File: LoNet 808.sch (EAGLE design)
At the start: 25 parts, among them CN2 JST-2.0, J4 MICRO-SMD, U1 TXB0104PWR

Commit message: add components
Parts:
- added C5: 470uf, Seeed-OPL-Capacitor:TANTALUM-SMD-470UF-6.3V(AVX-D)
- added C6: 220uf, Seeed-OPL-Capacitor:TANTALUM-SMD-220UF-16V(AVX-E)
- added D6: 28V-5A, Seeed-OPL-Diode:SMD-DIODE-SCHOTTKY-28V-5A(DO-214AA)
- added IC1: LM2596S, national-semiconductor:LM2596S
- added J5: DC-005, Seeed-OPL-Connector:CONN-POWER-JACK-2.1MM(DC-005)
- added L2: 22UH, Seeed-OPL-Inductor:SMD-INDUCTOR-22UH-20%(2P-2.0X1.2MM)
- added U2: (no value), LBRmicrobuilder:MCP73831/2
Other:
- note removed: "MICRO USB INTERFACE"
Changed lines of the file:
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@@
 <?xml version="1.0" encoding="utf-8"?>
 <!DOCTYPE eagle SYSTEM "eagle.dtd">
-<eagle version="6.5.0">
+<eagle version="7.5.0">
 <drawing>
 <settings>
@@
 <setting verticaltext="up"/>
 </settings>
-<grid distance="0.1" unitdist="inch" unit="mil" style="lines" multiple="1" display="no" altdistance="0.01" altunitdist="inch" altunit="inch"/>
+<grid distance="0.1" unitdist="inch" unit="inch" style="lines" multiple="1" display="no" altdistance="0.01" altunitdist="inch" altunit="inch"/>
 <layers>
 <layer number="1" name="Top" color="4" fill="1" visible="no" active="no"/>
@@
 <layer number="112" name="tSilk" color="7" fill="1" visible="no" active="yes"/>
 <layer number="113" name="IDFDebug" color="7" fill="1" visible="no" active="yes"/>
+<layer number="114" name="FRNTMAAT1" color="7" fill="1" visible="no" active="no"/>
+<layer number="115" name="FRNTMAAT2" color="7" fill="1" visible="no" active="no"/>
 <layer number="116" name="Patch_BOT" color="9" fill="4" visible="no" active="no"/>
+<layer number="117" name="BACKMAAT1" color="7" fill="1" visible="no" active="no"/>
 <layer number="118" name="Rect_Pads" color="7" fill="1" visible="no" active="no"/>
+<layer number="119" name="KAP_TEKEN" color="7" fill="1" visible="no" active="no"/>
+<layer number="120" name="KAP_MAAT1" color="7" fill="1" visible="no" active="no"/>
 <layer number="121" name="_tsilk" color="7" fill="1" visible="no" active="no"/>
 <layer number="122" name="_bsilk" color="7" fill="1" visible="no" active="no"/>
@@
 <layer number="127" name="_tValues" color="7" fill="1" visible="no" active="yes"/>
 <layer number="128" name="_bValues" color="7" fill="1" visible="no" active="yes"/>
+<layer number="129" name="top_silk" color="7" fill="1" visible="no" active="no"/>
+<layer number="130" name="SMDSTROOK" color="7" fill="1" visible="no" active="no"/>
 <layer number="131" name="tAdjust" color="7" fill="1" visible="no" active="yes"/>
 <layer number="132" name="bAdjust" color="7" fill="1" visible="no" active="yes"/>
+<layer number="133" name="bottom_silk" color="7" fill="1" visible="no" active="no"/>
 <layer number="144" name="DrillLegend" color="7" fill="1" visible="no" active="no"/>
 <layer number="150" name="Notes" color="7" fill="1" visible="no" active="yes"/>
@@
 <layer number="227" name="227bmp" color="7" fill="1" visible="no" active="yes"/>
 <layer number="228" name="228bmp" color="7" fill="1" visible="no" active="yes"/>
+<layer number="229" name="229bmp" color="7" fill="1" visible="no" active="no"/>
 <layer number="230" name="230bmp" color="7" fill="1" visible="no" active="yes"/>
+<layer number="231" name="Eagle3D_PG1" color="7" fill="1" visible="no" active="no"/>
+<layer number="232" name="Eagle3D_PG2" color="7" fill="1" visible="no" active="no"/>
+<layer number="233" name="Eagle3D_PG3" color="7" fill="1" visible="no" active="no"/>
 <layer number="248" name="Housing" color="7" fill="1" visible="no" active="yes"/>
 <layer number="249" name="Edge" color="7" fill="1" visible="no" active="yes"/>
@@
 <layer number="251" name="SMDround" color="12" fill="11" visible="no" active="no"/>
 <layer number="254" name="OrgLBR" color="13" fill="1" visible="no" active="no"/>
+<layer number="255" name="Accent" color="7" fill="1" visible="no" active="no"/>
 </layers>
 <schematic xreflabel="%F%N/%S.%C%R" xrefpart="/%S.%C%R">
@@
 <part name="J4" library="Connector" deviceset="USB-MICRO-5P" device="-SMD-THT" value="MICRO-SMD"/>
 <part name="FRAME1" library="Aesthetics" deviceset="FRAME-A4L" device=""/>
+<part name="U2" library="LBRmicrobuilder" deviceset="MCP73831/2" device=""/>
+<part name="J5" library="Seeed-OPL-Connector" deviceset="CONN-POWER-JACK-2.1MM(DC-005)" device="" value="DC-005"/>
+<part name="IC1" library="national-semiconductor" deviceset="LM2596" device="S"/>
+<part name="D6" library="Seeed-OPL-Diode" deviceset="SMD-DIODE-SCHOTTKY-28V-5A(DO-214AA)" device="" value="28V-5A"/>
+<part name="L2" library="Seeed-OPL-Inductor" deviceset="SMD-INDUCTOR-22UH-20%(2P-2.0X1.2MM)" device="" value="22UH"/>
+<part name="C5" library="Seeed-OPL-Capacitor" deviceset="TANTALUM-SMD-470UF-6.3V(AVX-D)" device="" value="470uf"/>
+<part name="C6" library="Seeed-OPL-Capacitor" deviceset="TANTALUM-SMD-220UF-16V(AVX-E)" device="" value="220uf"/>
 </parts>
 <sheets>
@@
 <plain>
 <text x="11.43" y="-288.29" size="2.54" layer="94">POWER SUPPLY</text>
-<text x="-176.022" y="-203.962" size="2.54" layer="94">MICRO USB INTERFACE</text>
 <text x="-72.39" y="-200.66" size="2.54" layer="94">SIMCARD SLOT</text>
 <text x="-81.28" y="-323.85" size="2.54" layer="94">POWER SWITCH</text>
@@
 <instance part="FRAME1" gate="G$1" x="-207.01" y="-331.47"/>
 <instance part="FRAME1" gate="G$2" x="-35.56" y="-331.47"/>
+<instance part="U2" gate="G$1" x="-121.92" y="-198.12"/>
+<instance part="J5" gate="JACK" x="-193.04" y="-195.58"/>
+<instance part="IC1" gate="G$1" x="-185.42" y="-213.36"/>
+<instance part="D6" gate="G$1" x="-157.48" y="-208.28"/>
+<instance part="L2" gate="L" x="-144.78" y="-215.9"/>
+<instance part="C5" gate="G$1" x="-213.36" y="-213.36"/>
+<instance part="C6" gate="G$1" x="-127" y="-218.44"/>
 </instances>
 <busses>

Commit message: add components
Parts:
- removed C5: 470uf, Seeed-OPL-Capacitor:TANTALUM-SMD-470UF-6.3V(AVX-D)
- removed C6: 220uf, Seeed-OPL-Capacitor:TANTALUM-SMD-220UF-16V(AVX-E)
- added CT1: 100UF, Seeed-OPL-Capacitor:ALUMINUM-SMD-100UF-50V-20%(D6MM)
- added CT2: 220UF, Seeed-OPL-Capacitor:ALUMINUM-SMD-220UF-16V(D6.3-H7.7MM)
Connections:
- new net N$1: CT1.+, IC1.VIN, J5.+
- new net N$2: D6.-, IC1.OUT, L2.1
- new net N$3: CT1.-, IC1.!ON!/OFF, IC1.GND, J5.-, J5.CDN
- new net N$5: CT2.-, D6.+
- new net N$7: CT2.+, IC1.FB, L2.2
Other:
- moved on the sheet: D6, IC1, J5, L2
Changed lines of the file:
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@@
 <setting verticaltext="up"/>
 </settings>
-<grid distance="0.1" unitdist="inch" unit="inch" style="lines" multiple="1" display="no" altdistance="0.01" altunitdist="inch" altunit="inch"/>
+<grid distance="25" unitdist="mil" unit="mil" style="lines" multiple="1" display="no" altdistance="0.01" altunitdist="inch" altunit="inch"/>
 <layers>
 <layer number="1" name="Top" color="4" fill="1" visible="no" active="no"/>
@@
 <part name="D6" library="Seeed-OPL-Diode" deviceset="SMD-DIODE-SCHOTTKY-28V-5A(DO-214AA)" device="" value="28V-5A"/>
 <part name="L2" library="Seeed-OPL-Inductor" deviceset="SMD-INDUCTOR-22UH-20%(2P-2.0X1.2MM)" device="" value="22UH"/>
-<part name="C5" library="Seeed-OPL-Capacitor" deviceset="TANTALUM-SMD-470UF-6.3V(AVX-D)" device="" value="470uf"/>
-<part name="C6" library="Seeed-OPL-Capacitor" deviceset="TANTALUM-SMD-220UF-16V(AVX-E)" device="" value="220uf"/>
+<part name="CT1" library="Seeed-OPL-Capacitor" deviceset="ALUMINUM-SMD-100UF-50V-20%(D6MM)" device="" value="100UF"/>
+<part name="CT2" library="Seeed-OPL-Capacitor" deviceset="ALUMINUM-SMD-220UF-16V(D6.3-H7.7MM)" device="" value="220UF"/>
 </parts>
 <sheets>
@@
 <instance part="FRAME1" gate="G$2" x="-35.56" y="-331.47"/>
 <instance part="U2" gate="G$1" x="-121.92" y="-198.12"/>
-<instance part="J5" gate="JACK" x="-193.04" y="-195.58"/>
-<instance part="IC1" gate="G$1" x="-185.42" y="-213.36"/>
-<instance part="D6" gate="G$1" x="-157.48" y="-208.28"/>
-<instance part="L2" gate="L" x="-144.78" y="-215.9"/>
-<instance part="C5" gate="G$1" x="-213.36" y="-213.36"/>
-<instance part="C6" gate="G$1" x="-127" y="-218.44"/>
+<instance part="J5" gate="JACK" x="-210.82" y="-195.58"/>
+<instance part="IC1" gate="G$1" x="-177.8" y="-198.12"/>
+<instance part="D6" gate="G$1" x="-160.02" y="-205.74" rot="R90"/>
+<instance part="L2" gate="L" x="-150.495" y="-195.58"/>
+<instance part="CT1" gate="G$1" x="-195.58" y="-198.12" rot="R270"/>
+<instance part="CT2" gate="G$1" x="-140.335" y="-205.74" rot="R270"/>
 </instances>
 <busses>
@@
 </segment>
 </net>
+<net name="N$1" class="0">
+<segment>
+<pinref part="J5" gate="JACK" pin="+"/>
+<pinref part="IC1" gate="G$1" pin="VIN"/>
+<wire x1="-204.47" y1="-193.04" x2="-195.58" y2="-193.04" width="0.1524" layer="91"/>
+<pinref part="CT1" gate="G$1" pin="+"/>
+<wire x1="-195.58" y1="-193.04" x2="-190.5" y2="-193.04" width="0.1524" layer="91"/>
+<wire x1="-195.58" y1="-194.31" x2="-195.58" y2="-193.04" width="0.1524" layer="91"/>
+<junction x="-195.58" y="-193.04"/>
+</segment>
+</net>
+<net name="N$3" class="0">
+<segment>
+<pinref part="IC1" gate="G$1" pin="!ON!/OFF"/>
+<pinref part="IC1" gate="G$1" pin="GND"/>
+<wire x1="-190.5" y1="-198.12" x2="-190.5" y2="-203.2" width="0.1524" layer="91"/>
+<wire x1="-190.5" y1="-203.2" x2="-190.5" y2="-205.74" width="0.1524" layer="91"/>
+<junction x="-190.5" y="-203.2"/>
+<pinref part="J5" gate="JACK" pin="CDN"/>
+<pinref part="J5" gate="JACK" pin="-"/>
+<wire x1="-204.47" y1="-195.58" x2="-204.47" y2="-198.12" width="0.1524" layer="91"/>
+<wire x1="-204.47" y1="-198.12" x2="-204.47" y2="-205.74" width="0.1524" layer="91"/>
+<junction x="-204.47" y="-198.12"/>
+<pinref part="CT1" gate="G$1" pin="-"/>
+<wire x1="-204.47" y1="-205.74" x2="-195.58" y2="-205.74" width="0.1524" layer="91"/>
+<wire x1="-195.58" y1="-205.74" x2="-195.58" y2="-201.93" width="0.1524" layer="91"/>
+<wire x1="-190.5" y1="-205.74" x2="-195.58" y2="-205.74" width="0.1524" layer="91"/>
+<junction x="-195.58" y="-205.74"/>
+</segment>
+</net>
+<net name="N$5" class="0">
+<segment>
+<wire x1="-195.58" y1="-206.375" x2="-195.58" y2="-210.185" width="0.1524" layer="91"/>
+<pinref part="CT2" gate="G$1" pin="-"/>
+<wire x1="-195.58" y1="-210.185" x2="-160.02" y2="-210.185" width="0.1524" layer="91"/>
+<wire x1="-160.02" y1="-210.185" x2="-140.335" y2="-210.185" width="0.1524" layer="91"/>
+<wire x1="-140.335" y1="-210.185" x2="-140.335" y2="-209.55" width="0.1524" layer="91"/>
+<pinref part="D6" gate="G$1" pin="+"/>
+<wire x1="-160.02" y1="-209.55" x2="-160.02" y2="-210.185" width="0.1524" layer="91"/>
+<junction x="-160.02" y="-210.185"/>
+</segment>
+</net>
+<net name="N$2" class="0">
+<segment>
+<pinref part="IC1" gate="G$1" pin="OUT"/>
+<pinref part="L2" gate="L" pin="1"/>
+<wire x1="-165.1" y1="-195.58" x2="-160.02" y2="-195.58" width="0.1524" layer="91"/>
+<pinref part="D6" gate="G$1" pin="-"/>
+<wire x1="-160.02" y1="-195.58" x2="-155.575" y2="-195.58" width="0.1524" layer="91"/>
+<wire x1="-160.02" y1="-201.93" x2="-160.02" y2="-195.58" width="0.1524" layer="91"/>
+<junction x="-160.02" y="-195.58"/>
+</segment>
+</net>
+<net name="N$7" class="0">
+<segment>
+<pinref part="L2" gate="L" pin="2"/>
+<pinref part="CT2" gate="G$1" pin="+"/>
+<wire x1="-145.415" y1="-195.58" x2="-140.335" y2="-195.58" width="0.1524" layer="91"/>
+<wire x1="-140.335" y1="-195.58" x2="-140.335" y2="-200.66" width="0.1524" layer="91"/>
+<pinref part="IC1" gate="G$1" pin="FB"/>
+<wire x1="-140.335" y1="-200.66" x2="-140.335" y2="-201.93" width="0.1524" layer="91"/>
+<wire x1="-165.1" y1="-200.66" x2="-140.335" y2="-200.66" width="0.1524" layer="91"/>
+<junction x="-140.335" y="-200.66"/>
+</segment>
+</net>

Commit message: add more
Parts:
- added C5: 10uf, Seeed-OPL-Capacitor:CERAMIC-10UF-10V-10%-X5R(0603)
- added D7: YELLOW-0603, Seeed-OPL-Diode:SMD-LED-CLEAR-YELLOW(0603)
- added D9: GREEN-0603, Seeed-OPL-Diode:SMD-LED-CLEAR-GREEN(0603)
- added R1: 1K, Seeed-OPL-Resistor:SMD-RES-1K-1%-1/10W(0603)
- added R2: 470R, Seeed-OPL-Resistor:SMD-RES-470R-5%-1/10W(0603)
- added R3: 2K, Seeed-OPL-Resistor:SMD-RES-2K-1%-1/10W(0603)
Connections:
- removed net N$3: CT1.-, IC1.!ON!/OFF, IC1.GND, J5.-, J5.CDN
- new net N$11: R1.2, R2.2, U2.STAT
- new net N$12: D9.+, R1.1
- new net N$13: D7.-, R2.1
- new net N$14: R3.1, U2.PROG
- net GND: now also CT1.-, IC1.!ON!/OFF, IC1.GND, J5.-, J5.CDN
- net N$5: now also C5.1, D9.-, R3.2, U2.VSS
- net N$7: now also C5.2, D7.+, U2.VDD
- net VBAT: now also U2.VBAT
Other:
- moved on the sheet: U2

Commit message: add mcu
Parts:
- added U3: ATMEGA328P-AU-TQFP32, Seeed-OPL-ic:MCU-ATMEGA328P-AU(TQFP32)
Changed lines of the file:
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@@
 <setting verticaltext="up"/>
 </settings>
-<grid distance="25" unitdist="mil" unit="mil" style="lines" multiple="1" display="no" altdistance="0.01" altunitdist="inch" altunit="inch"/>
+<grid distance="0.1" unitdist="inch" unit="inch" style="lines" multiple="1" display="no" altdistance="0.01" altunitdist="inch" altunit="inch"/>
 <layers>
 <layer number="1" name="Top" color="4" fill="1" visible="no" active="no"/>
@@
 <part name="R2" library="Seeed-OPL-Resistor" deviceset="SMD-RES-470R-5%-1/10W(0603)" device="" value="470R"/>
 <part name="R3" library="Seeed-OPL-Resistor" deviceset="SMD-RES-2K-1%-1/10W(0603)" device="" value="2K"/>
+<part name="U3" library="Seeed-OPL-ic" deviceset="MCU-ATMEGA328P-AU(TQFP32)" device="" value="ATMEGA328P-AU-TQFP32"/>
 </parts>
 <sheets>
@@
 <instance part="R2" gate="G$1" x="-114.3" y="-199.39"/>
 <instance part="R3" gate="G$1" x="-78.105" y="-196.85"/>
+<instance part="U3" gate="U" x="101.6" y="-190.5"/>
 </instances>
 <busses>

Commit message: more connection
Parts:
- added C6: 100nf, Seeed-OPL-Capacitor:CERAMIC-100NF-50V-10%-X7R(0603)
- added D10: BLUE-0603, Seeed-OPL-Diode:SMD-LED-CLEAR-BLUE(0603)
- added R5: 1.5K, Seeed-OPL-Resistor:SMD-RES-1.5K-1%-1/10W(0603)
- added R6: 10K, Seeed-OPL-Resistor:SMD-RES-10K-1%-1/10W(0603)
- added U$23: RESONATORSMD, SparkFun:RESONATORSMD
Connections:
- removed net N$5 (its old number): C5.1, CT2.-, D6.+, D9.-, R3.2, U2.VSS
- new net N$11: C6.2, U3.AREF
- new net N$13: R5.1, U3.PB1(OC1A)
- new net N$14: D10.+, R5.2
- new net N$15: U$23.1, U3.PB6(XTAL1/TOSC1)
- new net N$16: U$23.3, U3.PB7(XTAL2/TOSC2)
- new net RST: R6.2, U3.PC6(/RESET)
- net GND: now also C5.1, C6.1, CT2.-, D10.-, D6.+, D9.-, R3.2, U$23.2, U2.VSS, U3.GND, U3.GND@1, U3.GND@2
- net VBAT: now also R6.1, U3.AVCC, U3.VCC@1, U3.VCC@2
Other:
- moved on the sheet: D7, R2, R3, U2

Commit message: more connection
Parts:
- removed C3: 1uF, Common:C-0603
- removed J3: (no value), Connector:HEADER-2P-65/35MIL
- removed J4: MICRO-SMD, Connector:USB-MICRO-5P-SMD-THT
- added C7: 100nf, Seeed-OPL-Capacitor:CERAMIC-100NF-50V-10%-X7R(0603)
- added JP1: (no value), SparkFun-Connectors:M06SIP
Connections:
- removed net H_VIO: J2.7, U1.VCCB
- removed net N$7: C5.2, CT2.+, D7.+, IC1.FB, L2.2, U2.VDD
- new net N$18: C7.1, JP1.6
- net GND: now also JP1.1; no longer C3.1, J3.1, J4.GND@1, J4.GND@2, J4.GND@3
- net H_RXD: now also JP1.5, U3.PD1(TXD)
- net H_TXD: now also JP1.4, U3.PD0(RXD)
- net RST: now also C7.2
- net VBAT: now also J2.7, U1.VCCB
- net VBUS: now also C5.2, CT2.+, D7.+, IC1.FB, JP1.3, L2.2, U2.VDD; no longer C3.2, J3.2, J4.VCC, U$1.VBUS

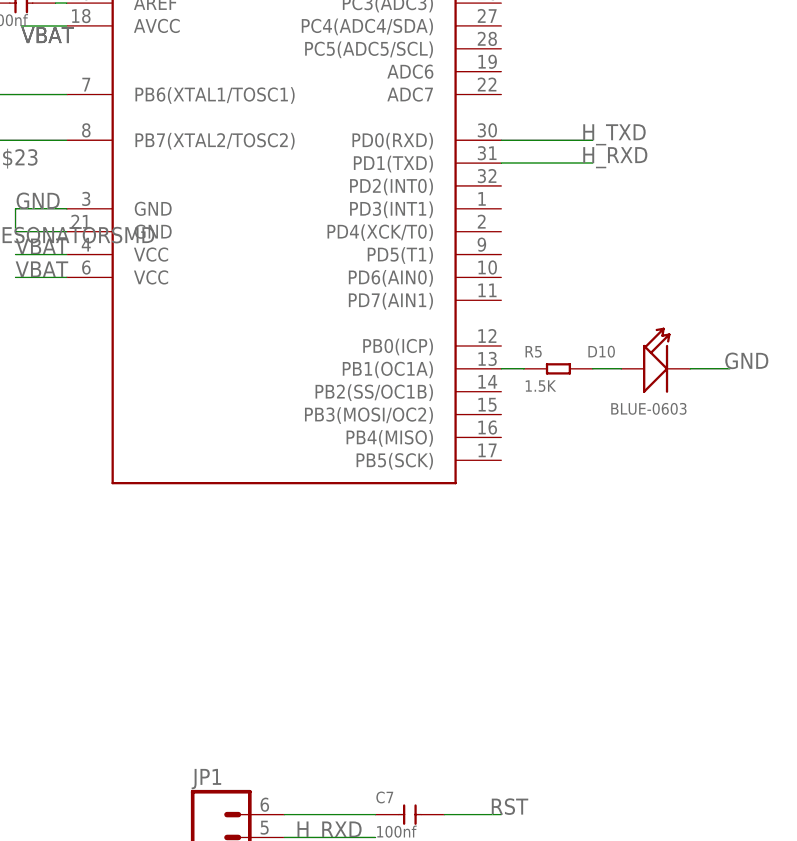
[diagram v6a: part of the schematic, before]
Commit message: add RFM83C
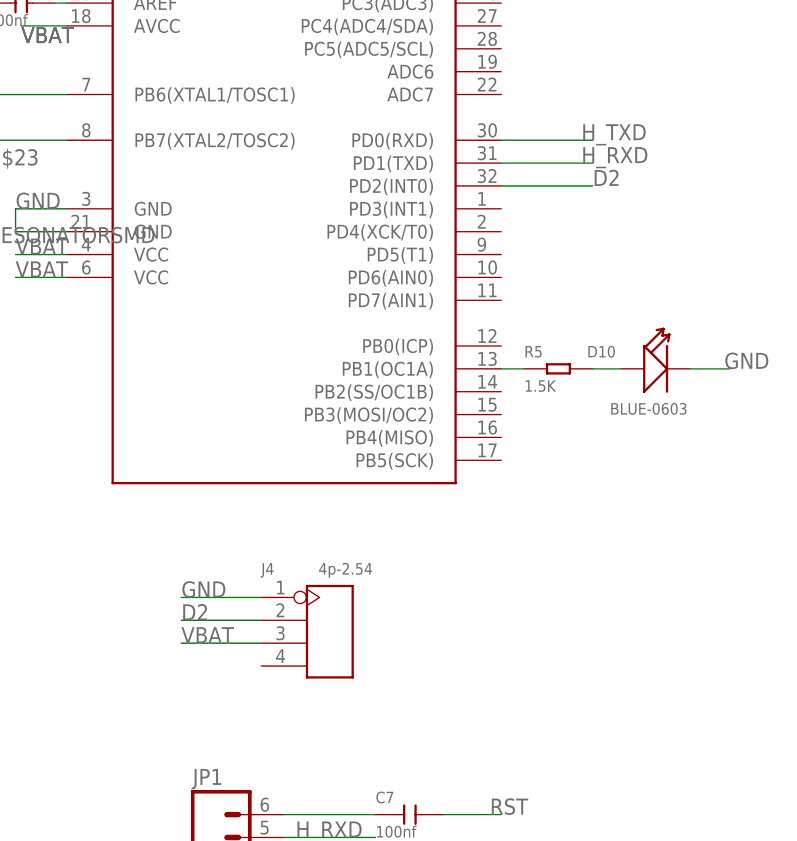
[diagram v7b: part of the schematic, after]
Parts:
- added J4: 4p-2.54, Seeed-OPL-Connector:DIP-BLACK-FEMALE-HEADER-VERT(4P-2.54)
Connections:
- new net D2: J4.P$2, U3.PD2(INT0)
- net GND: now also J4.P$1
- net VBAT: now also J4.P$3
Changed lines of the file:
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@@
 <part name="JP1" library="SparkFun-Connectors" deviceset="M06" device="SIP"/>
 <part name="C7" library="Seeed-OPL-Capacitor" deviceset="CERAMIC-100NF-50V-10%-X7R(0603)" device="" value="100nf"/>
+<part name="J4" library="Seeed-OPL-Connector" deviceset="DIP-BLACK-FEMALE-HEADER-VERT(4P-2.54)" device="" value="4p-2.54"/>
 </parts>
 <sheets>
@@
 <instance part="JP1" gate="G$1" x="96.52" y="-266.7"/>
 <instance part="C7" gate="G$1" x="115.57" y="-259.08"/>
+<instance part="J4" gate="G$1" x="106.68" y="-238.76"/>
 </instances>
 <busses>
@@
 <wire x1="-36.83" y1="-220.98" x2="-20.32" y2="-220.98" width="0.1524" layer="91"/>
 <label x="-30.48" y="-220.98" size="1.778" layer="95"/>
+</segment>
+<segment>
+<pinref part="J4" gate="G$1" pin="P$3"/>
+<wire x1="99.06" y1="-240.03" x2="90.17" y2="-240.03" width="0.1524" layer="91"/>
+<label x="90.17" y="-240.03" size="1.778" layer="95"/>
 </segment>
 </net>
@@
 <wire x1="104.14" y1="-271.78" x2="104.14" y2="-276.86" width="0.1524" layer="91"/>
 <label x="104.14" y="-276.86" size="1.778" layer="95"/>
+</segment>
+<segment>
+<pinref part="J4" gate="G$1" pin="P$1"/>
+<wire x1="99.06" y1="-234.95" x2="90.17" y2="-234.95" width="0.1524" layer="91"/>
+<label x="90.17" y="-234.95" size="1.778" layer="95"/>
 </segment>
 </net>
@@
 </segment>
 </net>
+<net name="D2" class="0">
+<segment>
+<pinref part="U3" gate="U" pin="PD2(INT0)"/>
+<wire x1="125.73" y1="-189.23" x2="135.89" y2="-189.23" width="0.1524" layer="91"/>
+<label x="135.89" y="-189.23" size="1.778" layer="95"/>
+</segment>
+<segment>
+<pinref part="J4" gate="G$1" pin="P$2"/>
+<wire x1="99.06" y1="-237.49" x2="90.17" y2="-237.49" width="0.1524" layer="91"/>
+<label x="90.17" y="-237.49" size="1.778" layer="95"/>
+</segment>
+</net>
